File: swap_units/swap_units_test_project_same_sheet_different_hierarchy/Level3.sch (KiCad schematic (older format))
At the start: 5 parts, among them U7 LM324

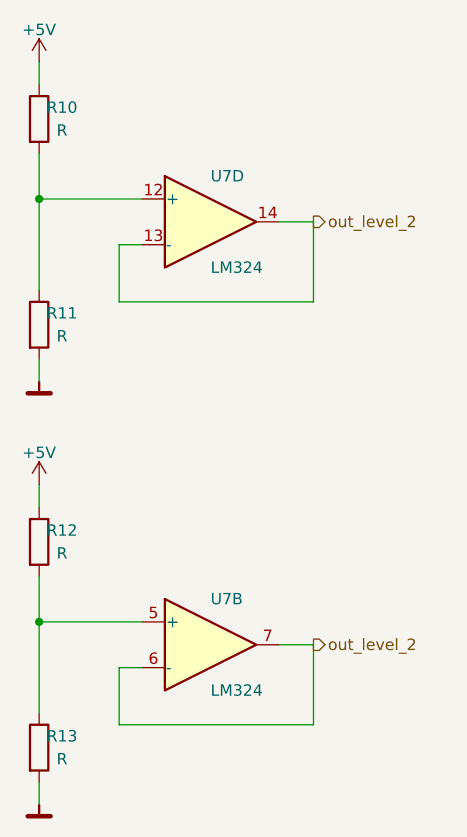
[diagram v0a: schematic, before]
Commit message: updated reference test projects
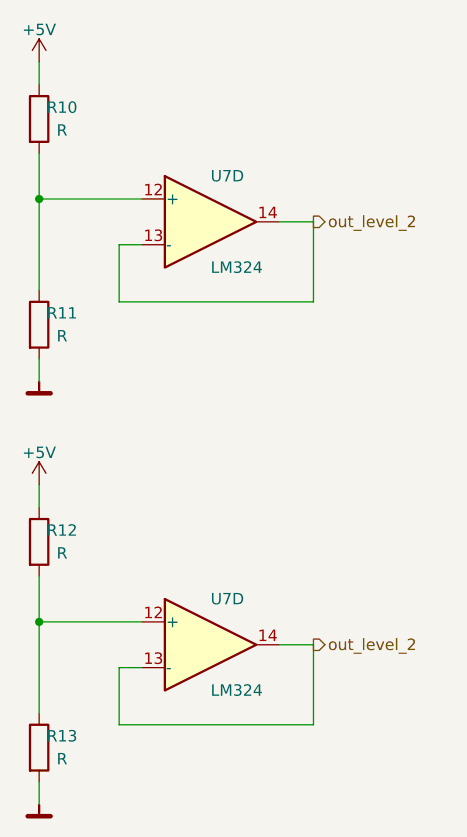
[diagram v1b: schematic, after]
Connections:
- net out_level_2: now also U7.13 (-), U7.14; no longer U7.6 (-), U7.7
- net at R12.2, R13.1: now also U7.12 (+); no longer U7.5 (+)
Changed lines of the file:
@@
 $Comp
 L Amplifier_Operational:LM324 U?
-U 2 1 5CB4FA1A
+U 4 1 5CB4FA1A
 P 3100 4300
-AR Path="/5B2A1286/5B2A1299/5CB4FA1A" Ref="U?"  Part="2"
-AR Path="/5B2A1286/5C9CDC4B/5CB4FA1A" Ref="U?"  Part="2"
-AR Path="/5B2A1286/5CB4DE53/5CB4FA1A" Ref="U7"  Part="2"
+AR Path="/5B2A1286/5B2A1299/5CB4FA1A" Ref="U?"  Part="4"
+AR Path="/5B2A1286/5C9CDC4B/5CB4FA1A" Ref="U?"  Part="4"
+AR Path="/5B2A1286/5CB4DE53/5CB4FA1A" Ref="U7"  Part="4"
 AR Path="/5B2A1286/5CB51184/5CB4FA1A" Ref="U8"  Part="2"
 F 0 "U7" H 3100 4500 50  0000 L CNN

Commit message: updated test projects
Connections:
- net out_level_2: no longer U7.13 (-), U7.14
- new net out_level_1: U7.13 (-), U7.14
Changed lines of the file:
@@
 	3550 4300 3400 4300
 Text HLabel 3550 4300 2    50   Output ~ 0
-out_level_2
+out_level_1
 $Comp
 L Amplifier_Operational:LM324 U7
